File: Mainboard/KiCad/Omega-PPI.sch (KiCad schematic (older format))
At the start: 11 parts, among them J11 KEYBOARD, U13 ATF16V8B, U2 82C55, U22 74HCT540, U23 74HCT273, U30 74HCT153, U31 74HCT153, U38 74AHCT32, U40 74HCT30, U41 74HCT30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

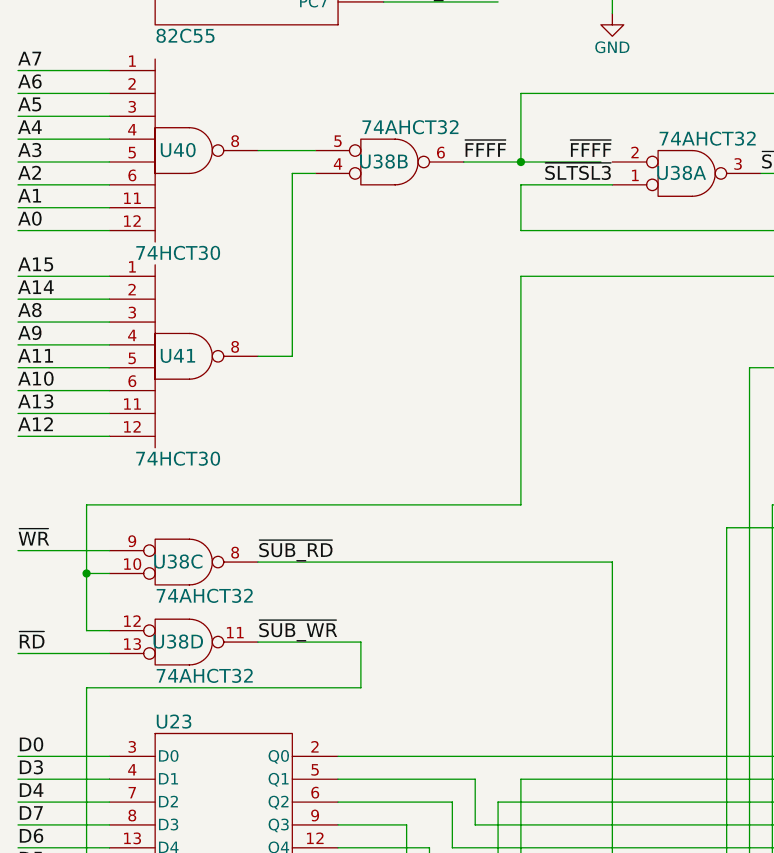
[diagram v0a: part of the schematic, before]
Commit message: Mainboard: Fix the issues discovered so far
Signed-off-by: Sergey Kiselev <skiselev@gmail.com>
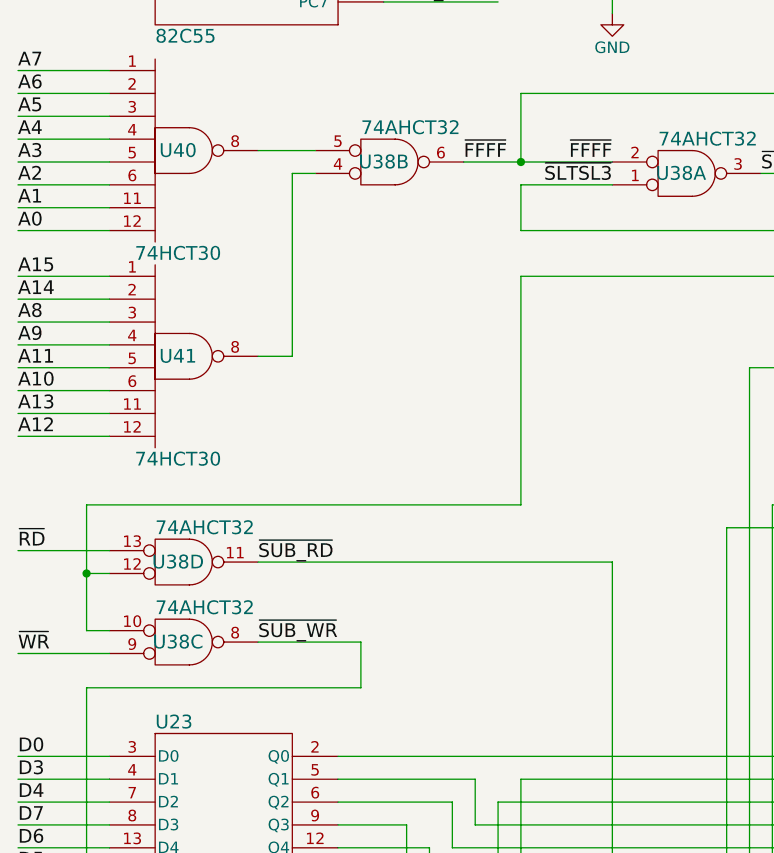
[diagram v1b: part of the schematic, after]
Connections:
- net ~SUB_RD: now also U38.11; no longer U38.8
- net ~SUB_WR: now also U38.8; no longer U38.11
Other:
- moved on the sheet: U38C, U38D
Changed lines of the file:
@@
-$Comp
-L my_components:74LS32 U38
-U 2 2 5A4E3627
-P 2300 3900
-F 0 "U38" H 2300 3900 60  0000 C CNN
-F 1 "74AHCT32" H 2200 3750 60  0000 L CNN
-F 2 "My_Components:IC_DIP14_300" H 2300 3900 60  0001 C CNN
-F 3 "" H 2300 3900 60  0000 C CNN
-	2    2300 3900
-	1    0    0    1
-$EndComp
 $Comp
 L my_components:74LS32 U38
@@
 	1    0    0    1
 $EndComp
-$Comp
-L my_components:74LS32 U38
-U 3 2 5BEB973E
-P 1400 5650
-F 0 "U38" H 1400 5650 60  0000 C CNN
-F 1 "74AHCT32" H 1300 5500 60  0000 L CNN
-F 2 "My_Components:IC_DIP14_300" H 1400 5650 60  0001 C CNN
-F 3 "" H 1400 5650 60  0000 C CNN
-	3    1400 5650
-	1    0    0    -1
-$EndComp
-$Comp
-L my_components:74LS32 U38
-U 4 2 5BEB9791
-P 1400 6000
-F 0 "U38" H 1400 6000 60  0000 C CNN
-F 1 "74AHCT32" H 1300 5850 60  0000 L CNN
-F 2 "My_Components:IC_DIP14_300" H 1400 6000 60  0001 C CNN
-F 3 "" H 1400 6000 60  0000 C CNN
-	4    1400 6000
-	1    0    0    -1
-$EndComp
+Text Label 700  5600 0    60   ~ 0
+~RD
 Text Label 700  6050 0    60   ~ 0
-~RD
-Text Label 700  5600 0    60   ~ 0
 ~WR
 $Comp
@@
 	5100 7500 5200 7500
 Wire Wire Line
-	2900 3900 3250 3900
+	2900 3900 3300 3900
 Wire Wire Line
 	1000 5700 1000 5950
@@
 Wire Wire Line
 	2900 6600 2900 7400
+$Comp
+L my_components:74LS32 U38
+U 3 2 5BEB973E
+P 1400 6000
+F 0 "U38" H 1400 6000 60  0000 C CNN
+F 1 "74AHCT32" H 1300 5850 60  0000 L CNN
+F 2 "My_Components:IC_DIP14_300" H 1400 6000 60  0001 C CNN
+F 3 "" H 1400 6000 60  0000 C CNN
+	3    1400 6000
+	1    0    0    1
+$EndComp
+$Comp
+L my_components:74LS32 U38
+U 2 2 5A4E3627
+P 2300 3900
+F 0 "U38" H 2300 3900 60  0000 C CNN
+F 1 "74AHCT32" H 2200 3750 60  0000 L CNN
+F 2 "My_Components:IC_DIP14_300" H 2300 3900 60  0001 C CNN
+F 3 "" H 2300 3900 60  0000 C CNN
+	2    2300 3900
+	1    0    0    1
+$EndComp
+$Comp
+L my_components:74LS32 U38
+U 4 2 5BEB9791
+P 1400 5650
+F 0 "U38" H 1400 5650 60  0000 C CNN
+F 1 "74AHCT32" H 1300 5500 60  0000 L CNN
+F 2 "My_Components:IC_DIP14_300" H 1400 5650 60  0001 C CNN
+F 3 "" H 1400 5650 60  0000 C CNN
+	4    1400 5650
+	1    0    0    1
+$EndComp
 $EndSCHEMATC

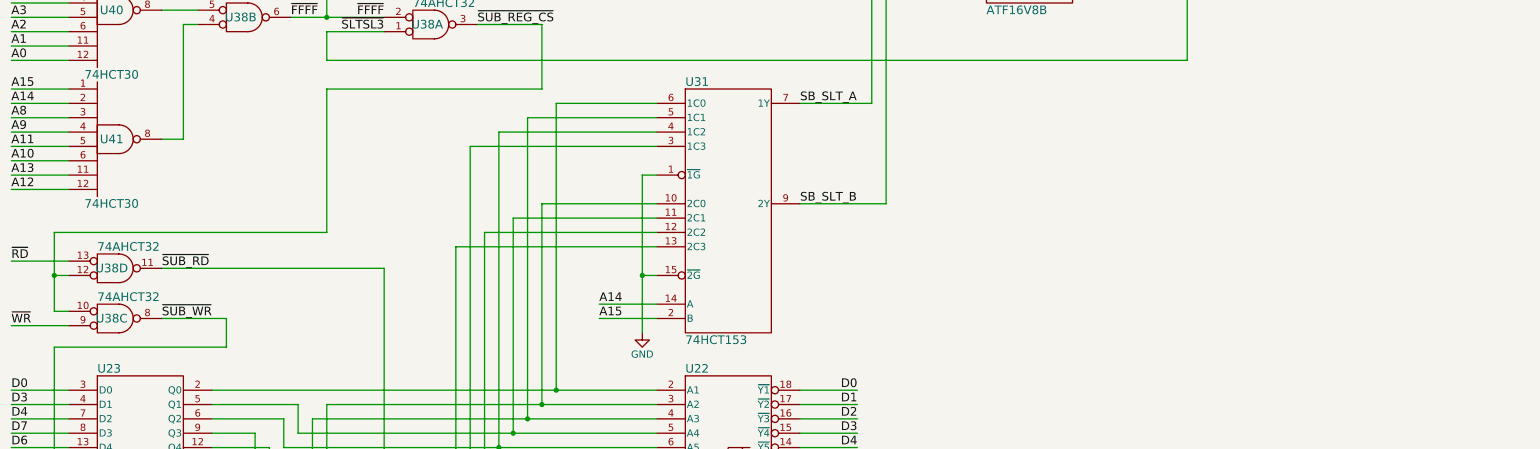
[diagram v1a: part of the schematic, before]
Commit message: Mainboard: Fixed schematic and PCB for v1.1
Signed-off-by: Sergey Kiselev <skiselev@gmail.com>
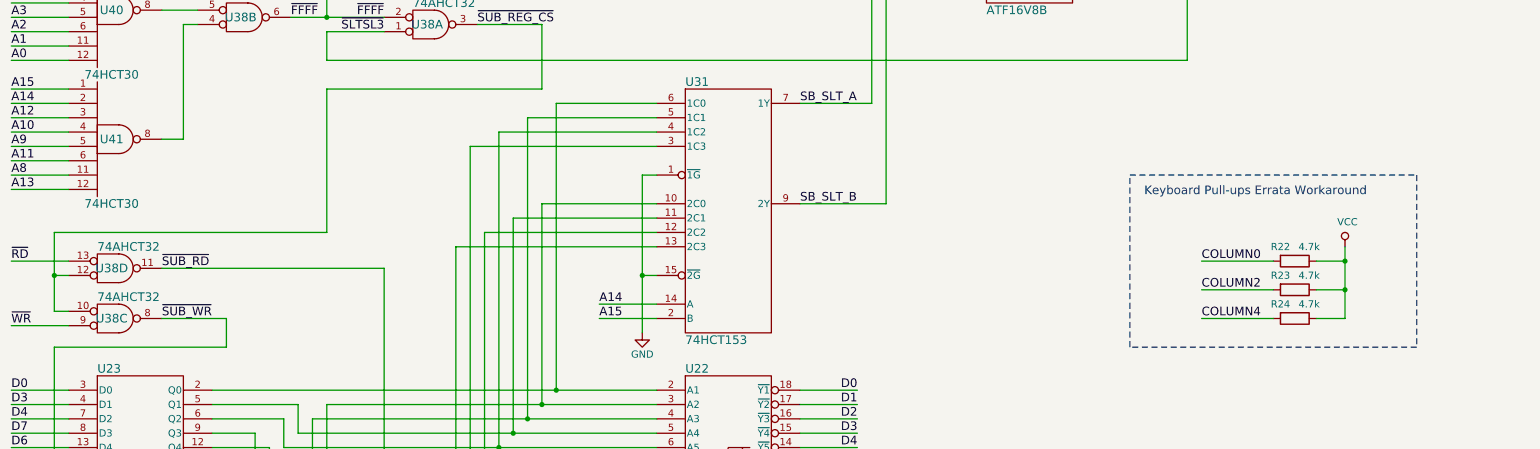
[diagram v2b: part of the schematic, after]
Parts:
- added R22, R23, R24: 4.7k, My_Components:Res_762, symbol Device:R
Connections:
- net A10: now also U41.4; no longer U41.6
- net A11: now also U41.6; no longer U41.5
- net A12: now also U41.3; no longer U41.12
- net A13: now also U41.12; no longer U41.11
- net A8: now also U41.11; no longer U41.3
- net A9: now also U41.5; no longer U41.4
- net COLUMN0: now also R22.2
- net COLUMN2: now also R23.2
- net COLUMN4: now also R24.2
- net VCC: now also R22.1, R23.1, R24.1
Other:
- note added: "Keyboard Pull-ups Errata Workaround"
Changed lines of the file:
@@
 Text Label 700  3500 0    60   ~ 0
 A7
+Text Label 700  5000 0    60   ~ 0
+A8
+Text Label 700  4800 0    60   ~ 0
+A9
+Text Label 700  4900 0    60   ~ 0
+A11
 Text Label 700  4600 0    60   ~ 0
-A8
-Text Label 700  4700 0    60   ~ 0
-A9
-Text Label 700  4800 0    60   ~ 0
-A11
+A12
 Text Label 700  5100 0    60   ~ 0
-A12
-Text Label 700  5000 0    60   ~ 0
 A13
 Text Label 700  4500 0    60   ~ 0
@@
 	1000 7400 1000 6200
 Wire Wire Line
-	3300 5650 3300 7500
-Wire Wire Line
 	6600 700  6200 700
 Wire Wire Line
@@
 	5200 6000 4800 6000
 Connection ~ 2900 3900
-Wire Wire Line
-	2200 6000 2200 6200
 Wire Wire Line
 	1750 6000 2200 6000
@@
 Wire Wire Line
 	1000 5700 1000 5950
-Text Label 700  4900 0    60   ~ 0
+Text Label 700  4700 0    60   ~ 0
 A10
 Wire Wire Line
@@
 	1    0    0    1
 $EndComp
+Wire Wire Line
+	2200 6000 2200 6200
+Wire Wire Line
+	3300 5650 3300 7500
+$Comp
+L Device:R R22
+U 1 1 5F651789
+P 9650 5600
+F 0 "R22" V 9550 5500 50  0000 C CNN
+F 1 "4.7k" V 9550 5700 50  0000 C CNN
+F 2 "My_Components:Res_762" V 9580 5600 50  0001 C CNN
+F 3 "~" H 9650 5600 50  0001 C CNN
+	1    9650 5600
+	0    1    1    0
+$EndComp
+$Comp
+L Device:R R23
+U 1 1 5F651EB8
+P 9650 5800
+F 0 "R23" V 9550 5700 50  0000 C CNN
+F 1 "4.7k" V 9550 5900 50  0000 C CNN
+F 2 "My_Components:Res_762" V 9580 5800 50  0001 C CNN
+F 3 "~" H 9650 5800 50  0001 C CNN
+	1    9650 5800
+	0    1    1    0
+$EndComp
+$Comp
+L Device:R R24
+U 1 1 5F652358
+P 9650 6000
+F 0 "R24" V 9550 5900 50  0000 C CNN
+F 1 "4.7k" V 9550 6100 50  0000 C CNN
+F 2 "My_Components:Res_762" V 9580 6000 50  0001 C CNN
+F 3 "~" H 9650 6000 50  0001 C CNN
+	1    9650 6000
+	0    1    1    0
+$EndComp
+Wire Wire Line
+	9500 5600 9000 5600
+Wire Wire Line
+	9500 5800 9000 5800
+Wire Wire Line
+	9500 6000 9000 6000
+Wire Wire Line
+	9800 5600 10000 5600
+Wire Wire Line
+	10000 5600 10000 5500
+Wire Wire Line
+	9800 5800 10000 5800
+Wire Wire Line
+	10000 5800 10000 5600
+Connection ~ 10000 5600
+Wire Wire Line
+	9800 6000 10000 6000
+Wire Wire Line
+	10000 6000 10000 5800
+Connection ~ 10000 5800
+$Comp
+L power:VCC #PWR02
+U 1 1 5F6C2774
+P 10000 5500
+F 0 "#PWR02" H 10000 5350 50  0001 C CNN
+F 1 "VCC" H 10017 5673 50  0000 C CNN
+F 2 "" H 10000 5500 50  0001 C CNN
+F 3 "" H 10000 5500 50  0001 C CNN
+	1    10000 5500
+	1    0    0    -1
+$EndComp
+Text Label 9000 5600 0    60   ~ 0
+COLUMN0
+Text Label 9000 5800 0    60   ~ 0
+COLUMN2
+Text Label 9000 6000 0    60   ~ 0
+COLUMN4
+Text Notes 8600 5150 0    60   ~ 0
+Keyboard Pull-ups Errata Workaround
+Wire Notes Line
+	8500 5000 10500 5000
+Wire Notes Line
+	10500 5000 10500 6200
+Wire Notes Line
+	10500 6200 8500 6200
+Wire Notes Line
+	8500 6200 8500 5000
 $EndSCHEMATC

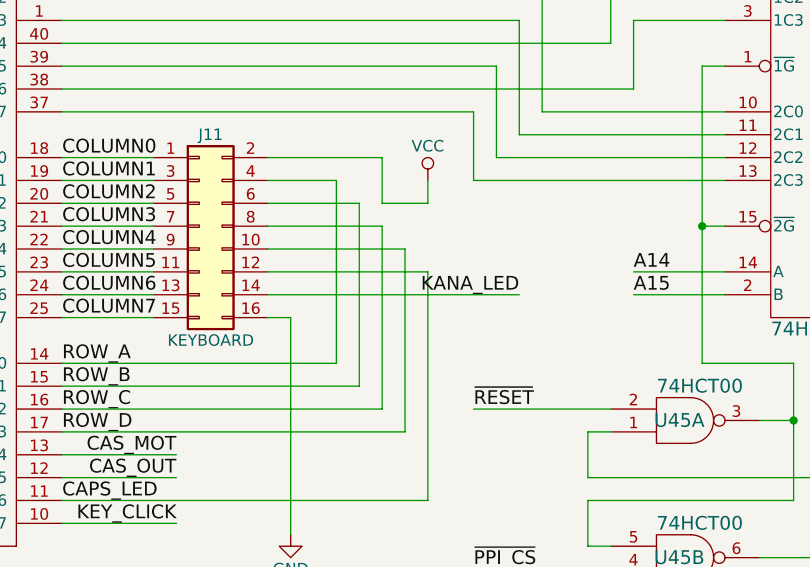
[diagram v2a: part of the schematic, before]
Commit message: Mainboard: Update schematic and PCB layout with latest fixes
Signed-off-by: Sergey Kiselev <skiselev@gmail.com>
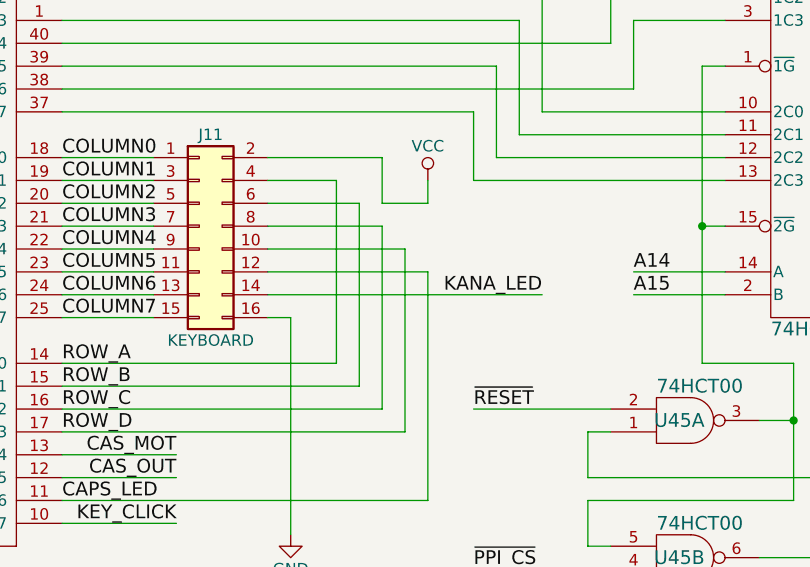
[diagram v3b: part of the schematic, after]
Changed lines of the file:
@@
 	1    0    0    -1
 $EndComp
-Text Label 4300 2200 2    60   ~ 0
+Text Label 4400 2200 2    60   ~ 0
 KANA_LED
 Text Label 9100 2900 0    60   ~ 0
@@
 	3900 2100 3900 3100
 Wire Wire Line
-	3200 2200 4300 2200
+	3200 2200 4400 2200
 Wire Wire Line
 	6600 3500 6600 700

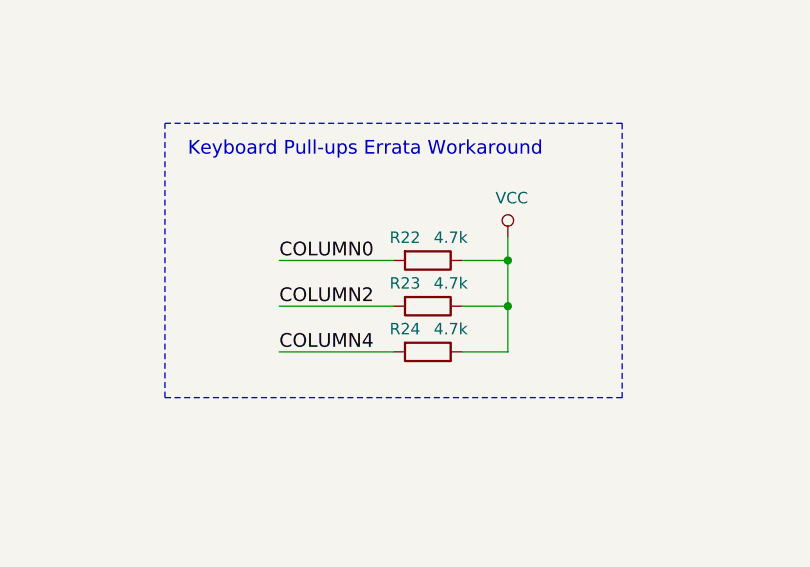
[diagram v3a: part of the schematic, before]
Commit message: Mainboard: Replace RGB and Cassette connectors with DIN8
Signed-off-by: Sergey Kiselev <skiselev@gmail.com>
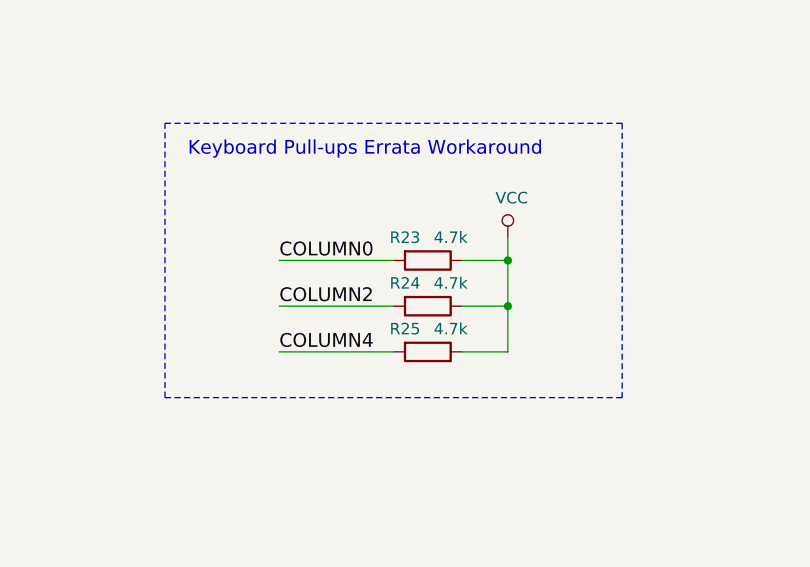
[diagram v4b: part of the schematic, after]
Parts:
- renumbered R22 to R23, R23 to R24, R24 to R25
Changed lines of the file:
@@
 	3300 5650 3300 7500
 $Comp
-L Device:R R22
+L Device:R R23
 U 1 1 5F651789
 P 9650 5600
-F 0 "R22" V 9550 5500 50  0000 C CNN
+F 0 "R23" V 9550 5500 50  0000 C CNN
 F 1 "4.7k" V 9550 5700 50  0000 C CNN
 F 2 "My_Components:Res_762" V 9580 5600 50  0001 C CNN
@@
 $EndComp
 $Comp
-L Device:R R23
+L Device:R R24
 U 1 1 5F651EB8
 P 9650 5800
-F 0 "R23" V 9550 5700 50  0000 C CNN
+F 0 "R24" V 9550 5700 50  0000 C CNN
 F 1 "4.7k" V 9550 5900 50  0000 C CNN
 F 2 "My_Components:Res_762" V 9580 5800 50  0001 C CNN
@@
 $EndComp
 $Comp
-L Device:R R24
+L Device:R R25
 U 1 1 5F652358
 P 9650 6000
-F 0 "R24" V 9550 5900 50  0000 C CNN
+F 0 "R25" V 9550 5900 50  0000 C CNN
 F 1 "4.7k" V 9550 6100 50  0000 C CNN
 F 2 "My_Components:Res_762" V 9580 6000 50  0001 C CNN
